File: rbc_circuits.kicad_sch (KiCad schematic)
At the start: 0 parts

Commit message: added mcu
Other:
- added sheet MCU (MCU.kicad_sch)
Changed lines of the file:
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@@
+    )
+  )
+  (sheet (at 78.74 124.46) (size 24.13 25.4) (fields_autoplaced)
+    (stroke (width 0.1524) (type solid))
+    (fill (color 0 0 0 0.0000))
+    (property "Sheetname" "MCU" (at 78.74 123.7484 0)
+      (effects (font (size 1.27 1.27)) (justify left bottom))
+    )
+    (property "Sheetfile" "MCU.kicad_sch" (at 78.74 150.4446 0)
+      (effects (font (size 1.27 1.27)) (justify left top))
+    )
+    (instances
+      (project "rbc_circuits"
+        (path "/1df96114-eb1a-4ddf-9ea3-acd2b4d12bf3" (page "6"))
+      )
     )
   )

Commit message: MCU migration completed
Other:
- title: (none) -> RBC by UGS
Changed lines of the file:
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@@
 (kicad_sch (version 20230121) (generator eeschema)
   (paper "A4")
+  (title_block
+    (title "RBC by UGS")
+    (date "2023-09-04")
+    (rev "2.0")
+  )
   (sheet (at 116.84 87.63) (size 25.4 25.4) (fields_autoplaced)
     (stroke (width 0.1524) (type solid))

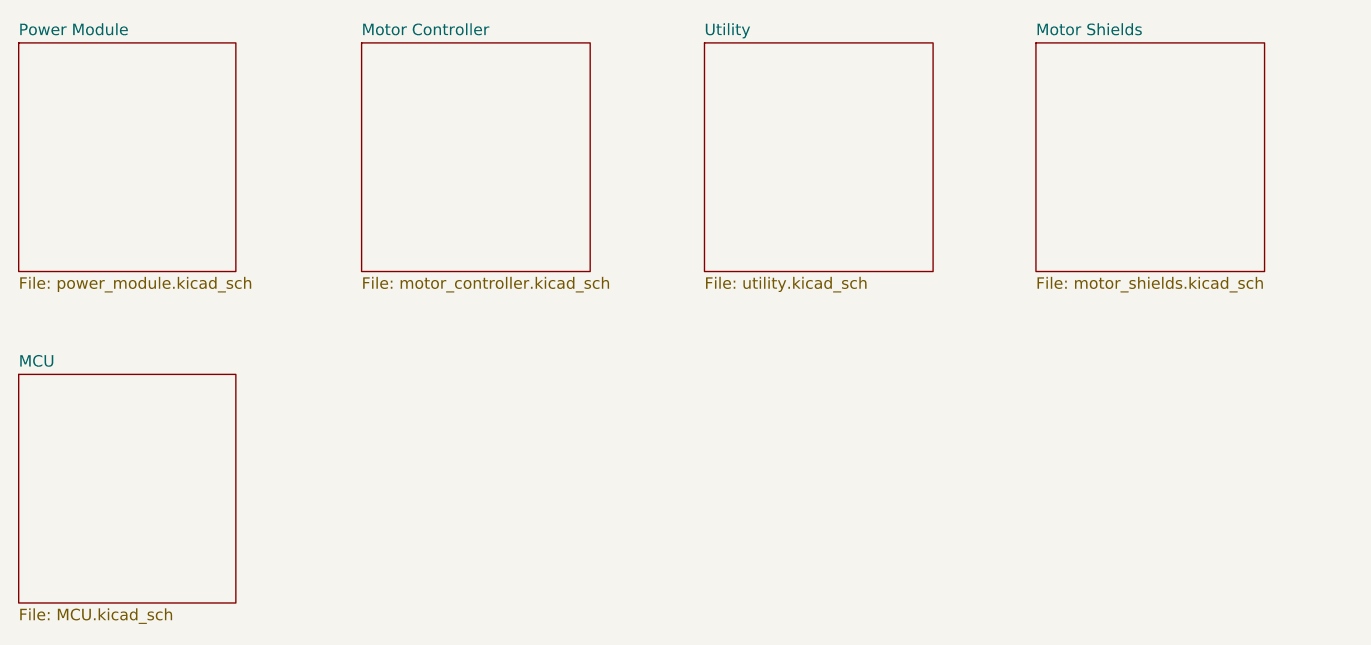
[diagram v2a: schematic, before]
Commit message: removed arduino mega
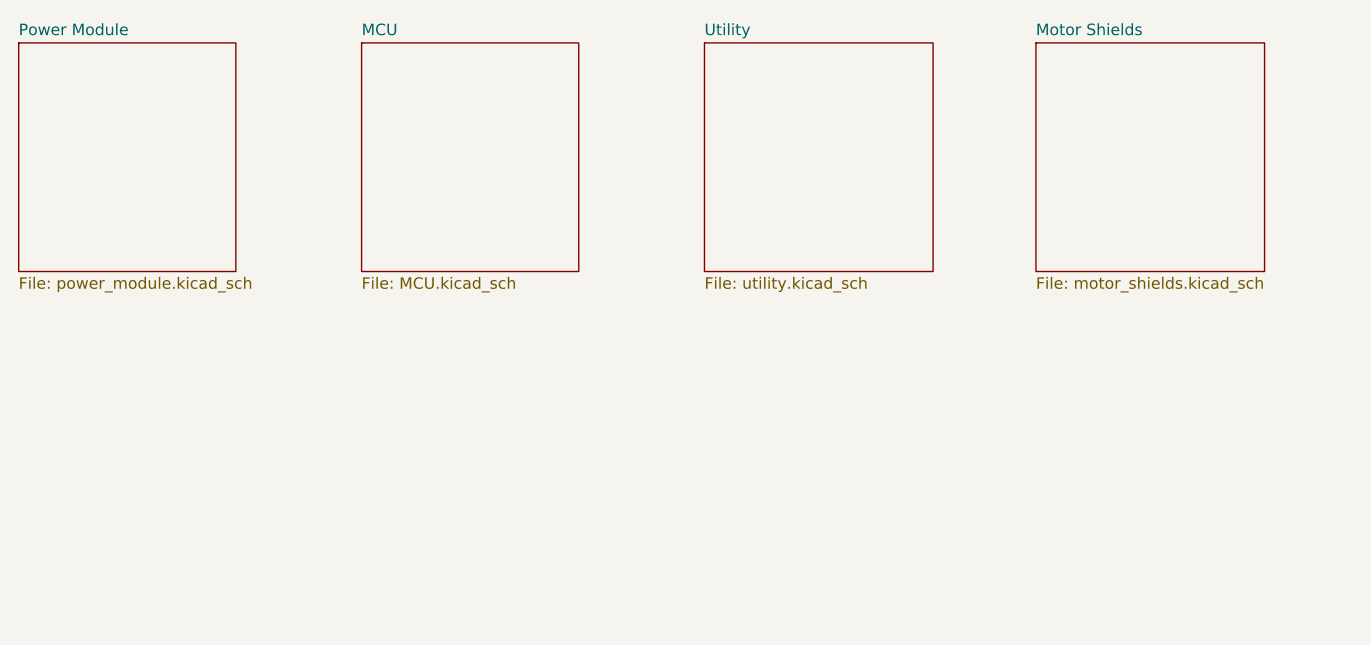
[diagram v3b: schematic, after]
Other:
- removed sheet Motor Controller
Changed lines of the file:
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@@
     (rev "2.0")
-  )
-  (sheet (at 116.84 87.63) (size 25.4 25.4) (fields_autoplaced)
-    (stroke (width 0.1524) (type solid))
-    (fill (color 0 0 0 0.0000))
-    (property "Sheetname" "Motor Controller" (at 116.84 86.9184 0)
-      (effects (font (size 1.27 1.27)) (justify left bottom))
-    )
-    (property "Sheetfile" "motor_controller.kicad_sch" (at 116.84 113.6146 0)
-      (effects (font (size 1.27 1.27)) (justify left top))
-    )
-    (instances
-      (project "rbc_circuits"
-        (path "/1df96114-eb1a-4ddf-9ea3-acd2b4d12bf3" (page "3"))
-      )
-    )
   )
   (sheet (at 154.94 87.63) (size 25.4 25.4) (fields_autoplaced)
@@
     )
   )
-  (sheet (at 78.74 124.46) (size 24.13 25.4) (fields_autoplaced)
+  (sheet (at 116.84 87.63) (size 24.13 25.4) (fields_autoplaced)
     (stroke (width 0.1524) (type solid))
     (fill (color 0 0 0 0.0000))
-    (property "Sheetname" "MCU" (at 78.74 123.7484 0)
+    (property "Sheetname" "MCU" (at 116.84 86.9184 0)
       (effects (font (size 1.27 1.27)) (justify left bottom))
     )
-    (property "Sheetfile" "MCU.kicad_sch" (at 78.74 150.4446 0)
+    (property "Sheetfile" "MCU.kicad_sch" (at 116.84 113.6146 0)
       (effects (font (size 1.27 1.27)) (justify left top))
     )
